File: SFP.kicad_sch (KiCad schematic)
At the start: 45 parts, among them J6 Bel-Fuse_SFP+_1x20_SS-79100-0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, U13 PCA9539AHF

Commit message: [#81970] Finalize connecting SFP+ to SOM
[#82054] Update SoM pins definitions

[#82054] Continue work on I2C

[#82330] Clean up

[#81970] Add SFP sheet and power section

[#82330] Annotation and clean up
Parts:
- removed C208, C209, C210, C211, C212, C213, C214, C215, C78, C80, C81, C82: C_100n_0402, antmicro-footprints:C_0402_1005Metric, symbol antmicroCapacitors0402:C_100n_0402
- removed C79: C_22u_16V_0603, antmicro-footprints:C_0603_1608Metric, symbol antmicroCapacitors0603:C_22u_16V_0603
- removed D15: LED_Y_0603_LTST-C191KSKT, antmicro-footprints:LED_0603_1608Metric_Y, symbol antmicroLEDIndicationDiscrete:LED_Y_0603_LTST-C191KSKT
- removed D16: LED_G_0603_LTST-C190GKT, antmicro-footprints:LED_0603_1608Metric_G, symbol antmicroLEDIndicationDiscrete:LED_G_0603_LTST-C190GKT
- removed J6: Bel-Fuse_SFP+_1x20_SS-79100-001, antmicro-footprints:Conn_Bel-Fuse_SFP+_1x20_SS-79100-001, symbol antmicroWire2BoardConnectors:Bel-Fuse_SFP+_1x20_SS-79100-001
- removed R100, R101, R102, R99: R_1k_0402, antmicro-footprints:R_0402_1005Metric, symbol antmicroResistors0402:R_1k_0402
- removed R103, R104, R84, R85, R86, R87, R88, R89, R90, R91, R92, R96, R97, R98: R_0R_0402, antmicro-footprints:R_0402_1005Metric, symbol antmicroResistors0402:R_0R_0402
- removed R105: R_330R_0402, antmicro-footprints:R_0402_1005Metric, symbol antmicroResistors0402:R_330R_0402
- removed R106, R107: R_220R_0402, antmicro-footprints:R_0402_1005Metric, symbol antmicroResistors0402:R_220R_0402
- removed TP13, TP14, TP15, TP16, TP17, TP18, TP19: TP_0.75mm_SMD, antmicro-footprints:TP_SMD_0.75mm, symbol antmicroTestPoints:TP_0.75mm_SMD
- removed U13: PCA9539AHF, antmicro-footprints:QFN-24-1EP_4x4mm_P0.5_EP2.1x2.1mm, symbol antmicroInterfaceIOExpanders:PCA9539AHF
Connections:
- no-connect marks 9 -> 0
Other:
- note removed: "Address 0x75"
- note removed: "Conects to ~{PERST} on root schematics"
- note removed: "Depending if we will have enough GPIO we can swap expander for direct GPIO connection to LEDs"
- note removed: "Grounded within the module How to connect it? GPIO?"
- note removed: "How to get MAC addres?"
- note removed: "SFP+"
- note removed: "SFP+ indicator LEDs GPIO expander"
- note removed: "What about MDIO?"

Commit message: [#81970] Create basic connections to the SFP+ connector
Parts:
- added C208, C209, C210, C211, C212, C213, C214, C215, C78, C80, C81, C82: C_100n_0402, antmicro-footprints:C_0402_1005Metric, symbol antmicroCapacitors0402:C_100n_0402
- added C79: C_22u_16V_0603, antmicro-footprints:C_0603_1608Metric, symbol antmicroCapacitors0603:C_22u_16V_0603
- added D15: LED_Y_0603_LTST-C191KSKT, antmicro-footprints:LED_0603_1608Metric_Y, symbol antmicroLEDIndicationDiscrete:LED_Y_0603_LTST-C191KSKT
- added D16: LED_G_0603_LTST-C190GKT, antmicro-footprints:LED_0603_1608Metric_G, symbol antmicroLEDIndicationDiscrete:LED_G_0603_LTST-C190GKT
- added J6: Bel-Fuse_SFP+_1x20_SS-79100-001, antmicro-footprints:Conn_Bel-Fuse_SFP+_1x20_SS-79100-001, symbol antmicroWire2BoardConnectors:Bel-Fuse_SFP+_1x20_SS-79100-001
- added R100, R101, R102, R99: R_1k_0402, antmicro-footprints:R_0402_1005Metric, symbol antmicroResistors0402:R_1k_0402
- added R103, R104, R84, R85, R86, R87, R88, R89, R90, R91, R92, R96, R97, R98: R_0R_0402, antmicro-footprints:R_0402_1005Metric, symbol antmicroResistors0402:R_0R_0402
- added R105: R_330R_0402, antmicro-footprints:R_0402_1005Metric, symbol antmicroResistors0402:R_330R_0402
- added R106, R107: R_220R_0402, antmicro-footprints:R_0402_1005Metric, symbol antmicroResistors0402:R_220R_0402
- added TP13, TP14, TP15, TP16, TP17, TP18, TP19: TP_0.75mm_SMD, antmicro-footprints:TP_SMD_0.75mm, symbol antmicroTestPoints:TP_0.75mm_SMD
- added U13: PCA9539AHF, antmicro-footprints:QFN-24-1EP_4x4mm_P0.5_EP2.1x2.1mm, symbol antmicroInterfaceIOExpanders:PCA9539AHF
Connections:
- new net: J6.8 (RX_{LOS}), R101.1, TP16.1
- new net: J6.6 (MOD_{ABS}), R102.1, R98.2
- new net: TP17.1, U13.6 (IO0_5)
- new net: TP13.1, U13.4 (IO0_3)
- new net: R87.2, U13.19 (SCL)
- new net: J6.2 (TX_{FAULT}), R100.1, TP15.1
- new net: J6.3 (TX_{DISABLE}), R103.1
- new net: J6.7 (RS0), R99.1
- new net: J6.9 (RS1), R104.1
- new net: R84.1, R85.2, U13.18 (A0)
- new net: R86.2, U13.20 (SDA)
- new net: R89.2, U13.23 (A1)
- new net: R88.2, U13.24 (~{RESET})
- new net: TP14.1, U13.5 (IO0_4)
- new net: TP18.1, U13.7 (IO0_6)
- new net: TP19.1, U13.8 (IO0_7)
- new net: D16.1 (C), R107.2
- new net: D15.1 (C), R106.2
- new net +3V3: C78.2, C79.2, C80.2, C81.2, D15.2 (A), D16.2 (A), J6.15 (V_{CC}(R)), J6.16 (V_{CC}(T)), R100.2, R101.2, R102.2, R84.2, R99.2, U13.21 (VDD)
- new net GND: C208.2, C209.2, C210.2, C211.2, C212.2, C213.2, C214.2, C215.2, C78.1, C79.1, C80.1, C81.1, C82.2, J6.1 (V_{EE}(T)), J6.10 (V_{EE}(R)), J6.11 (V_{EE}(R)), J6.14 (V_{EE}(R)), J6.17 (V_{EE}(T)), J6.20 (V_{EE}(T)), R103.2, R104.2, R105.2, R85.1, R89.1, U13.25 (GND), U13.9 (GND)
- new net I2C_{LED}.SCL: R87.1
- new net I2C_{LED}.SDA: R86.1
- new net I2C_{SFP0}.SCL: R97.1
- new net I2C_{SFP0}.SDA: R96.1
- new net MOD0_ABS: R98.1
- new net SCL0: J6.5 (SCL), R97.2
- new net SDA0: J6.4 (SDA), R96.2
- new net SFI0.RX+: J6.13 (RD+)
- new net SFI0.RX-: J6.12 (RD-)
- new net SFI0.TX+: J6.18 (TD+)
- new net SFI0.TX-: J6.19 (TD-)
- new net SFP0_LEDG: R107.1, R91.2, R92.2
- new net SFP0_LEDY: R106.1, R90.2
- new net SH: C208.1, C209.1, C210.1, C211.1, C212.1, C213.1, C214.1, C215.1, C82.1, J6.SH, R105.1
- new net ~{LED0_0}: R90.1, U13.1 (IO0_0)
- new net ~{LED0_1}: R91.1, U13.2 (IO0_1)
- new net ~{LED0_2}: R92.1, U13.3 (IO0_2)
- new net ~{RESET}: R88.1
- no-connect marks 0 -> 9
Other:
- note added: "Address 0x75"
- note added: "Connect to: UPHY_TX6_N K16 UPHY_TX6_P K17 UPHY_RX6_N B17 UPHY_RX6_P B16"
- note added: "SFP+"

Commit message: [#81970] Work on SFP+ status LEDs
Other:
- note added: "Depending if we will have enough GPIO we can swap expander for direct GPIO connection to LEDs"
- note added: "SFP+ indicator LEDs GPIO expander"
- moved on the sheet: C78, R84, R85, R86, R87, R88, R89, R90, R91, R92, TP13, TP14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

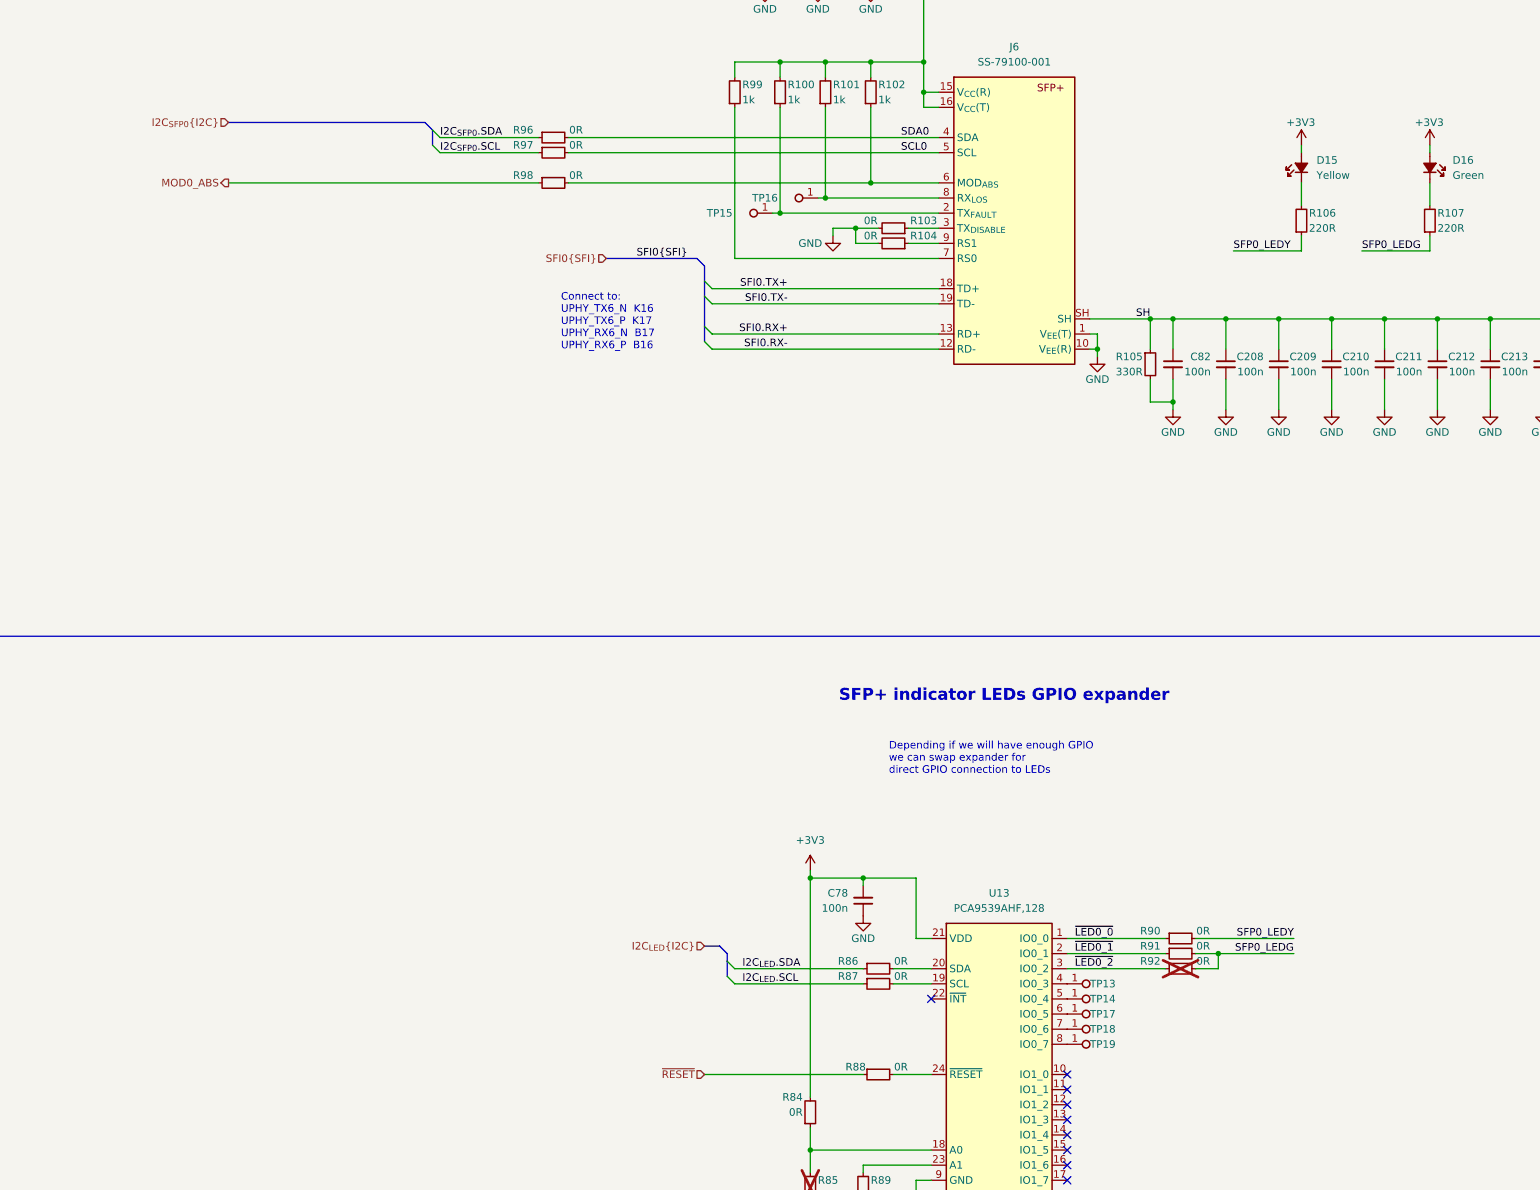
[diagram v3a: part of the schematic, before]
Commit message: [#81970] Connect SFI to SOM
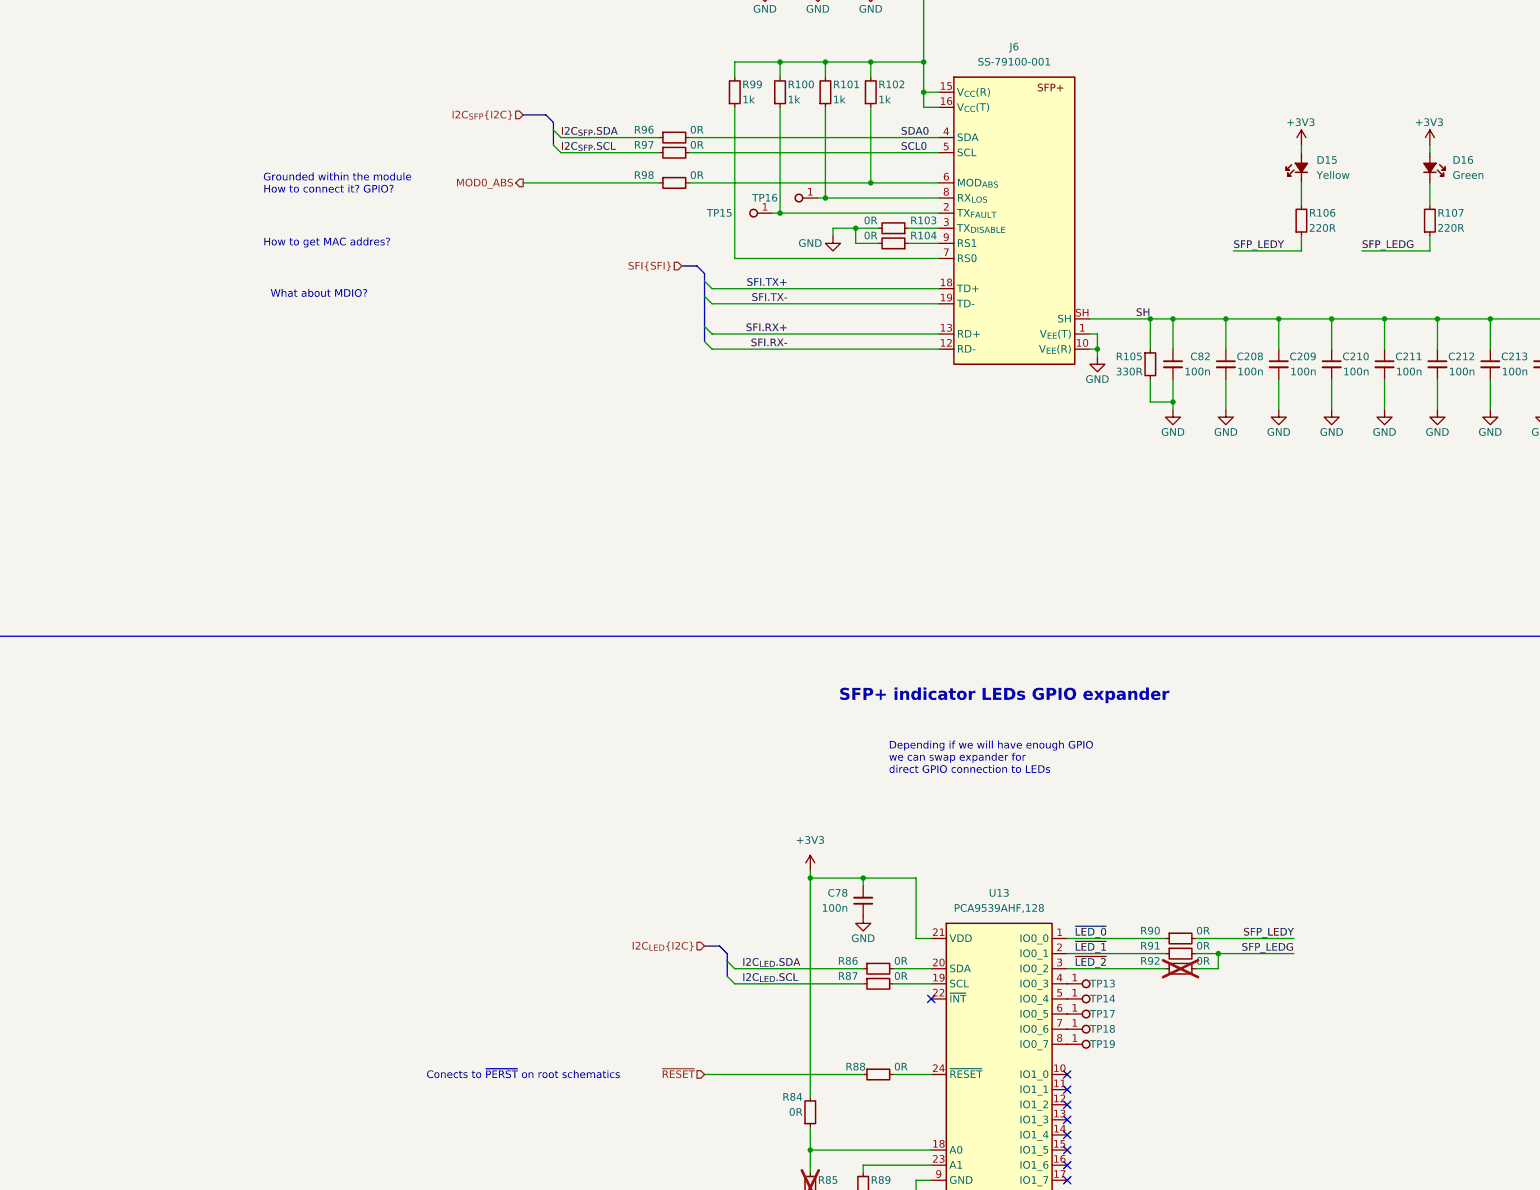
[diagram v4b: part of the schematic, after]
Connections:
- net I2C_{SFP0}.SCL renamed I2C_{SFP}.SCL
- net I2C_{SFP0}.SDA renamed I2C_{SFP}.SDA
- net SFI0.RX+ renamed SFI.RX+
- net SFI0.RX- renamed SFI.RX-
- net SFI0.TX+ renamed SFI.TX+
- net SFI0.TX- renamed SFI.TX-
- net SFP0_LEDG renamed SFP_LEDG
- net SFP0_LEDY renamed SFP_LEDY
- net ~{LED0_0} renamed ~{LED_0}
- net ~{LED0_1} renamed ~{LED_1}
- net ~{LED0_2} renamed ~{LED_2}
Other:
- note added: "Conects to ~{PERST} on root schematics"
- note added: "Grounded within the module How to connect it? GPIO?"
- note added: "How to get MAC addres?"
- note added: "What about MDIO?"
- note removed: "Connect to: UPHY_TX6_N K16 UPHY_TX6_P K17 UPHY_RX6_N B17 UPHY_RX6_P B16"
- moved on the sheet: R96, R97, R98
